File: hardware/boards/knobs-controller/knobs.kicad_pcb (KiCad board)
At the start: 2 copper layers, 110.5 x 54.3 mm, 70 parts, among them J1 ZX62-AB-5PA(31), J4 JST---S4B-PH-SM4-TB(LF)(SN)_J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, J8 2X3_SMD_MALE, SW1 Rotary Encoder, SW2 Rotary Encoder, SW3 Rotary Encoder, U2 AP7215-33YG-13, U3 ATSAMD21G18A-48, Y1 32.768KHz

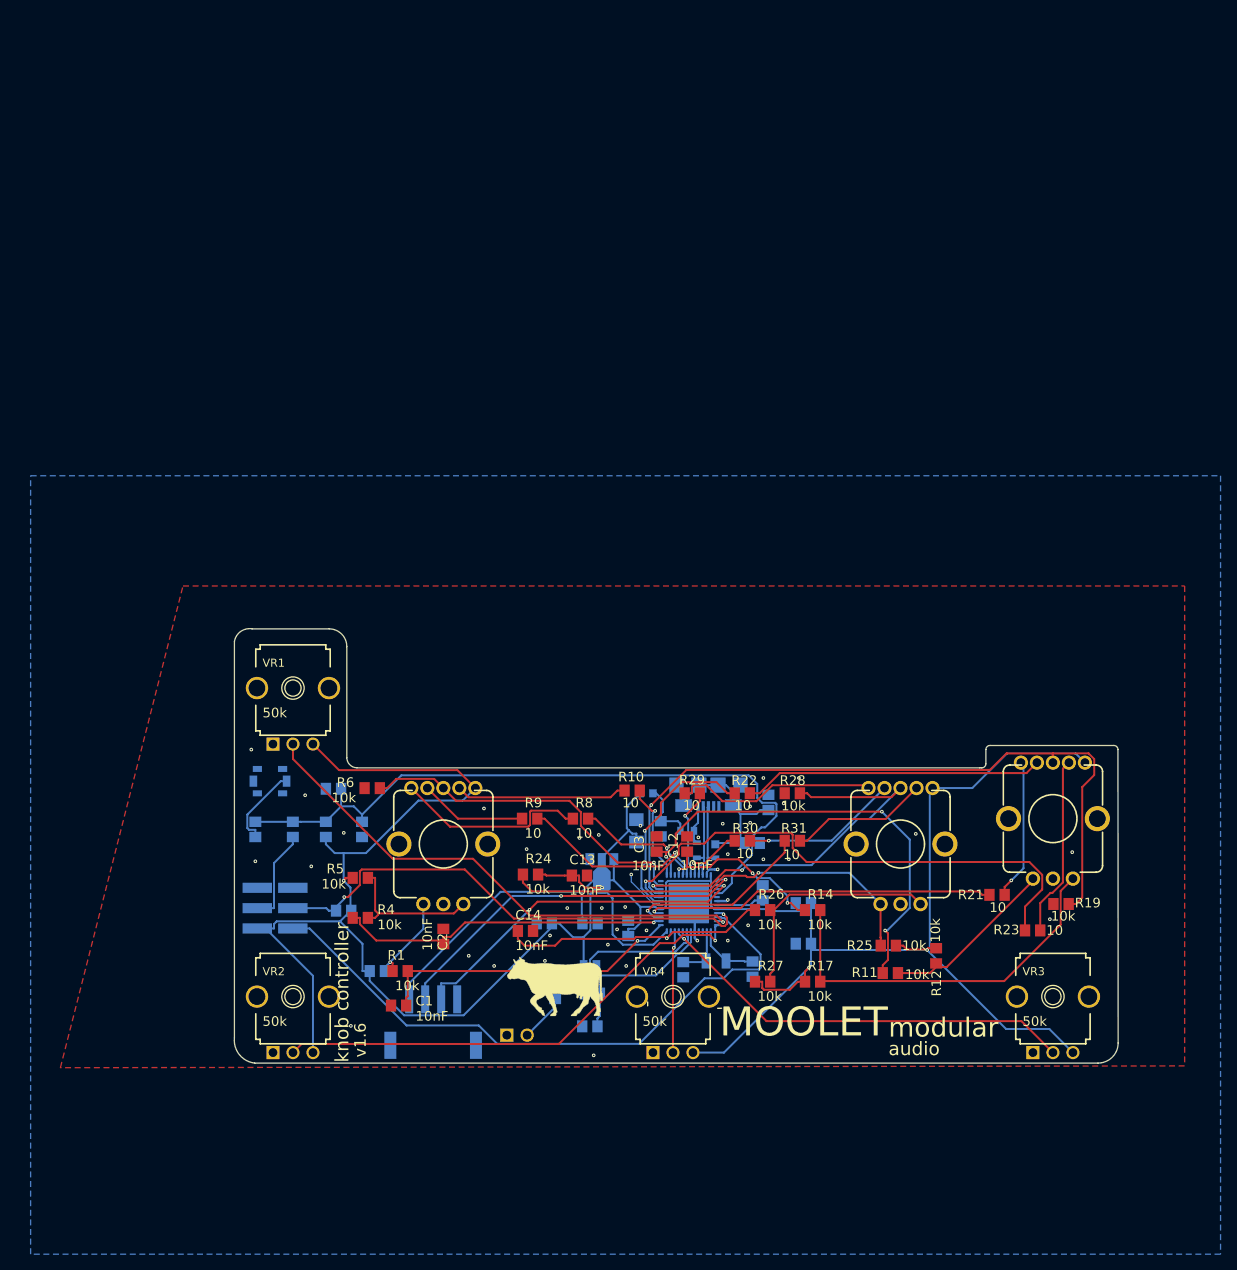
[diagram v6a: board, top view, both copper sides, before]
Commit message: v1.7: merge knobs and top breakout in to single board, remove fpc connector, replace with standard 0.1' pin header
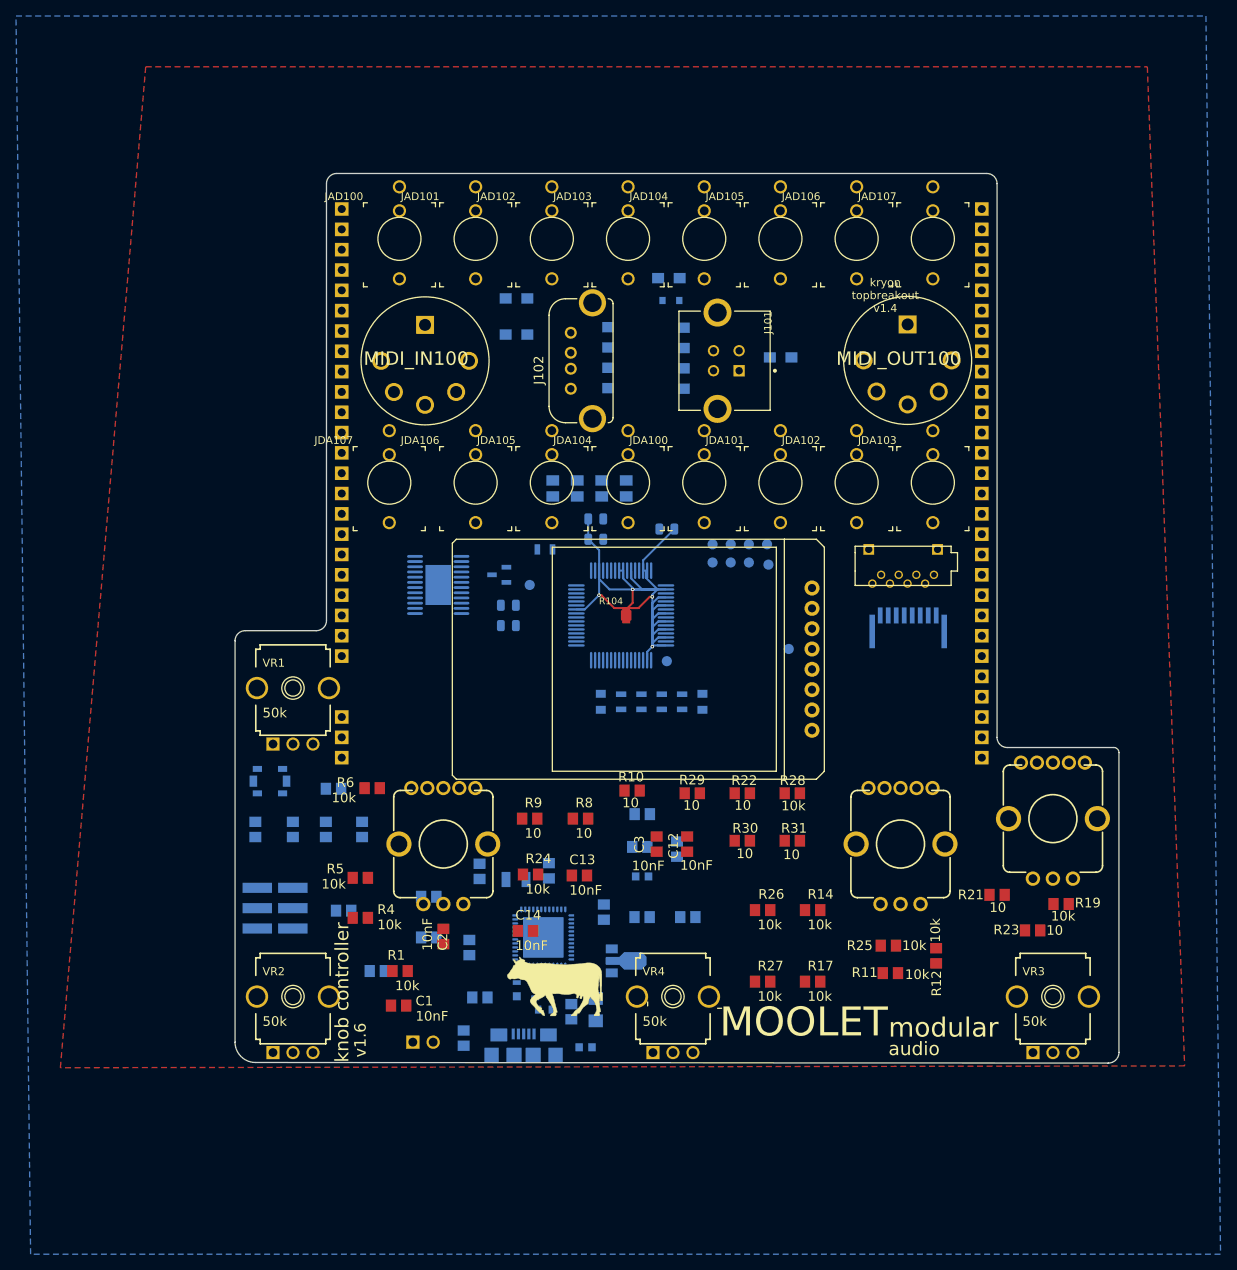
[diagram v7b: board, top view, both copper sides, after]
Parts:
- added C100: 0.1u, topbreakout:C0805K, B.Cu at (139.2, 60.3)
- added C101: 0.1u, topbreakout:C0805K, B.Cu at (136.1, 60.3)
- added C102: 0.1u, topbreakout:C0805K, B.Cu at (142.2, 60.3)
- added C103: 0.1u, topbreakout:C0805K, B.Cu at (133.1, 60.3)
- added C104: 10uF, Capacitor_SMD:C_0805_2012Metric, B.Cu at (147.3, 65.4)
- added C105: 1.0uF, Capacitor_SMD:C_0805_2012Metric, B.Cu at (138.4, 66.7)
- added C106: 1.0uF, Capacitor_SMD:C_0805_2012Metric, B.Cu at (138.4, 64.1)
- added C107: 0.1uF, Capacitors_SMD:C_0805, B.Cu at (139.1, 87.0)
- added C108: 0.1uF, Capacitors_SMD:C_0805, B.Cu at (151.8, 87.0)
- added C109: 0.1uF, Capacitor_SMD:C_0805_2012Metric, B.Cu at (127.5, 77.5)
- added C110: 0.1uF, Capacitor_SMD:C_0805_2012Metric, B.Cu at (127.5, 74.9)
- added D100: D, Diodes_SMD:D_0805, B.Cu at (147.8, 36.8)
- added J10: Conn_01x01_Female, Connector_PinSocket_2.54mm:PinSocket_1x01_P2.54mm_Vertical, B.Cu at (106.7, 48.3)
- added J101: WURTH_ELECTRONICS_61400413321WURTH_ELECTRONICS_61400413321_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, topbreakout:WURTH_ELECTRONICS_61400413321_0, F.Cu at (154.5, 44.4)
- added J102: USB-A-S-X-X-VT, topbreakout:USB-A-S-X-X-VT, F.Cu at (138.0, 44.4)
- added J103: ST7735_1.4, topbreakout:ST7735, F.Cu at (167.0, 66.7)
- added J11: Conn_01x01_Female, Connector_PinSocket_2.54mm:PinSocket_1x01_P2.54mm_Vertical, B.Cu at (186.7, 61.0)
- added J12: Conn_01x01_Female, Connector_PinSocket_2.54mm:PinSocket_1x01_P2.54mm_Vertical, B.Cu at (106.7, 63.5)
- added J13: Conn_01x01_Female, Connector_PinSocket_2.54mm:PinSocket_1x01_P2.54mm_Vertical, B.Cu at (106.7, 58.4)
- added J14: Conn_01x01_Female, Connector_PinSocket_2.54mm:PinSocket_1x01_P2.54mm_Vertical, B.Cu at (106.7, 81.3)
- added J15: Conn_01x01_Female, Connector_PinSocket_2.54mm:PinSocket_1x01_P2.54mm_Vertical, B.Cu at (106.7, 53.3)
- added J16: Conn_01x01_Female, Connector_PinSocket_2.54mm:PinSocket_1x01_P2.54mm_Vertical, B.Cu at (186.7, 76.2)
- added J17: Conn_01x01_Female, Connector_PinSocket_2.54mm:PinSocket_1x01_P2.54mm_Vertical, B.Cu at (186.7, 81.3)
- added J18: Conn_01x01_Female, Connector_PinSocket_2.54mm:PinSocket_1x01_P2.54mm_Vertical, B.Cu at (106.7, 66.0)
- added J19: Conn_01x01_Female, Connector_PinSocket_2.54mm:PinSocket_1x01_P2.54mm_Vertical, B.Cu at (186.7, 63.5)
- added J2: Conn_01x01_Female, Connector_PinSocket_2.54mm:PinSocket_1x01_P2.54mm_Vertical, B.Cu at (186.7, 50.8)
- added J20: Conn_01x01_Female, Connector_PinSocket_2.54mm:PinSocket_1x01_P2.54mm_Vertical, B.Cu at (186.7, 71.1)
- added J21: Conn_01x01_Female, Connector_PinSocket_2.54mm:PinSocket_1x01_P2.54mm_Vertical, B.Cu at (186.7, 68.6)
- added J22: Conn_01x01_Female, Connector_PinSocket_2.54mm:PinSocket_1x01_P2.54mm_Vertical, B.Cu at (186.7, 66.0)
- added J23: Conn_01x01_Female, Connector_PinSocket_2.54mm:PinSocket_1x01_P2.54mm_Vertical, B.Cu at (186.7, 73.7)
- added J24: Conn_01x01_Female, Connector_PinSocket_2.54mm:PinSocket_1x01_P2.54mm_Vertical, B.Cu at (106.7, 55.9)
- added J25: Conn_01x01_Female, Connector_PinSocket_2.54mm:PinSocket_1x01_P2.54mm_Vertical, B.Cu at (186.7, 83.8)
- added J26: Conn_01x01_Female, Connector_PinSocket_2.54mm:PinSocket_1x01_P2.54mm_Vertical, B.Cu at (186.7, 78.7)
- added J27: Conn_01x01_Female, Connector_PinSocket_2.54mm:PinSocket_1x01_P2.54mm_Vertical, B.Cu at (106.7, 61.0)
- added J28: Conn_01x01_Female, Connector_PinSocket_2.54mm:PinSocket_1x01_P2.54mm_Vertical, B.Cu at (106.7, 71.1)
- added J29: Conn_01x01_Female, Connector_PinSocket_2.54mm:PinSocket_1x01_P2.54mm_Vertical, B.Cu at (106.7, 73.7)
- added J3: Conn_01x01_Female, Connector_PinSocket_2.54mm:PinSocket_1x01_P2.54mm_Vertical, B.Cu at (186.7, 53.3)
- added J30: Conn_01x01_Female, Connector_PinSocket_2.54mm:PinSocket_1x01_P2.54mm_Vertical, B.Cu at (106.7, 68.6)
- added J31: Conn_01x01_Female, Connector_PinSocket_2.54mm:PinSocket_1x01_P2.54mm_Vertical, B.Cu at (106.7, 78.7)
- added J32: Conn_01x01_Female, Connector_PinSocket_2.54mm:PinSocket_1x01_P2.54mm_Vertical, B.Cu at (106.7, 76.2)
- added J33: Conn_01x01_Female, Connector_PinSocket_2.54mm:PinSocket_1x01_P2.54mm_Vertical, B.Cu at (186.7, 58.4)
- added J34: Conn_01x01_Female, Connector_PinSocket_2.54mm:PinSocket_1x01_P2.54mm_Vertical, B.Cu at (186.7, 94.0)
- added J35: Conn_01x01_Female, Connector_PinSocket_2.54mm:PinSocket_1x01_P2.54mm_Vertical, B.Cu at (186.7, 91.4)
- added J36: Conn_01x01_Female, Connector_PinSocket_2.54mm:PinSocket_1x01_P2.54mm_Vertical, B.Cu at (186.7, 88.9)
- added J37: Conn_01x01_Female, Connector_PinSocket_2.54mm:PinSocket_1x01_P2.54mm_Vertical, B.Cu at (186.7, 38.1)
- added J38: Conn_01x01_Female, Connector_PinSocket_2.54mm:PinSocket_1x01_P2.54mm_Vertical, B.Cu at (186.7, 40.6)
- added J39: Conn_01x01_Female, Connector_PinSocket_2.54mm:PinSocket_1x01_P2.54mm_Vertical, B.Cu at (186.7, 35.6)
- added J40: Conn_01x01_Female, Connector_PinSocket_2.54mm:PinSocket_1x01_P2.54mm_Vertical, B.Cu at (186.7, 43.2)
- added J41: Conn_01x01_Female, Connector_PinSocket_2.54mm:PinSocket_1x01_P2.54mm_Vertical, B.Cu at (186.7, 30.5)
- added J42: Conn_01x01_Female, Connector_PinSocket_2.54mm:PinSocket_1x01_P2.54mm_Vertical, B.Cu at (106.7, 88.9)
- added J43: Conn_01x01_Female, Connector_PinSocket_2.54mm:PinSocket_1x01_P2.54mm_Vertical, B.Cu at (186.7, 45.7)
- added J44: Conn_01x01_Female, Connector_PinSocket_2.54mm:PinSocket_1x01_P2.54mm_Vertical, B.Cu at (186.7, 33.0)
- added J45: Conn_01x01_Female, Connector_PinSocket_2.54mm:PinSocket_1x01_P2.54mm_Vertical, B.Cu at (106.7, 91.4)
- added J46: Conn_01x01_Female, Connector_PinSocket_2.54mm:PinSocket_1x01_P2.54mm_Vertical, B.Cu at (106.7, 27.9)
- added J47: Conn_01x01_Female, Connector_PinSocket_2.54mm:PinSocket_1x01_P2.54mm_Vertical, B.Cu at (186.7, 48.3)
- added J48: Conn_01x01_Female, Connector_PinSocket_2.54mm:PinSocket_1x01_P2.54mm_Vertical, B.Cu at (106.7, 94.0)
- added J49: Conn_01x01_Female, Connector_PinSocket_2.54mm:PinSocket_1x01_P2.54mm_Vertical, B.Cu at (106.7, 35.1)
- added J5: Conn_01x01_Female, Connector_PinSocket_2.54mm:PinSocket_1x01_P2.54mm_Vertical, B.Cu at (186.7, 55.9)
- added J50: Conn_01x01_Female, Connector_PinSocket_2.54mm:PinSocket_1x01_P2.54mm_Vertical, B.Cu at (106.7, 25.4)
- added J51: Conn_01x01_Female, Connector_PinSocket_2.54mm:PinSocket_1x01_P2.54mm_Vertical, B.Cu at (186.7, 25.4)
- added J52: Conn_01x01_Female, Connector_PinSocket_2.54mm:PinSocket_1x01_P2.54mm_Vertical, B.Cu at (106.7, 40.6)
- added J53: Conn_01x01_Female, Connector_PinSocket_2.54mm:PinSocket_1x01_P2.54mm_Vertical, B.Cu at (106.7, 33.0)
- added J54: Conn_01x01_Female, Connector_PinSocket_2.54mm:PinSocket_1x01_P2.54mm_Vertical, B.Cu at (106.7, 30.5)
- added J55: Conn_01x01_Female, Connector_PinSocket_2.54mm:PinSocket_1x01_P2.54mm_Vertical, B.Cu at (186.7, 27.9)
- added J56: Conn_01x01_Female, Connector_PinSocket_2.54mm:PinSocket_1x01_P2.54mm_Vertical, B.Cu at (106.7, 38.1)
- added J6: Conn_01x01_Female, Connector_PinSocket_2.54mm:PinSocket_1x01_P2.54mm_Vertical, B.Cu at (106.7, 45.7)
- added J7: Conn_01x01_Female, Connector_PinSocket_2.54mm:PinSocket_1x01_P2.54mm_Vertical, B.Cu at (106.7, 43.2)
- added J9: Conn_01x01_Female, Connector_PinSocket_2.54mm:PinSocket_1x01_P2.54mm_Vertical, B.Cu at (106.7, 50.8)
- added JAD100: THONKICONNNEW, topbreakout:WQP-PJ301M-12_JACK, F.Cu at (113.9, 29.1)
- added JAD101: THONKICONNNEW, topbreakout:WQP-PJ301M-12_JACK, F.Cu at (123.4, 29.1)
- added JAD102: THONKICONNNEW, topbreakout:WQP-PJ301M-12_JACK, F.Cu at (132.9, 29.1)
- added JAD103: THONKICONNNEW, topbreakout:WQP-PJ301M-12_JACK, F.Cu at (142.5, 29.1)
- added JAD104: THONKICONNNEW, topbreakout:WQP-PJ301M-12_JACK, F.Cu at (152.0, 29.1)
- added JAD105: THONKICONNNEW, topbreakout:WQP-PJ301M-12_JACK, F.Cu at (161.5, 29.1)
- added JAD106: THONKICONNNEW, topbreakout:WQP-PJ301M-12_JACK, F.Cu at (171.0, 29.1)
- added JAD107: THONKICONNNEW, topbreakout:WQP-PJ301M-12_JACK, F.Cu at (180.6, 29.1)
- added JDA100: THONKICONNNEW, topbreakout:WQP-PJ301M-12_JACK, F.Cu at (152.0, 59.6)
- added JDA101: THONKICONNNEW, topbreakout:WQP-PJ301M-12_JACK, F.Cu at (161.5, 59.6)
- added JDA102: THONKICONNNEW, topbreakout:WQP-PJ301M-12_JACK, F.Cu at (171.0, 59.6)
- added JDA103: THONKICONNNEW, topbreakout:WQP-PJ301M-12_JACK, F.Cu at (180.6, 59.6)
- added JDA104: THONKICONNNEW, topbreakout:WQP-PJ301M-12_JACK, F.Cu at (142.5, 59.6)
- added JDA105: THONKICONNNEW, topbreakout:WQP-PJ301M-12_JACK, F.Cu at (132.9, 59.6)
- added JDA106: THONKICONNNEW, topbreakout:WQP-PJ301M-12_JACK, F.Cu at (123.4, 59.6)
- added JDA107: THONKICONNNEW, topbreakout:WQP-PJ301M-12_JACK, F.Cu at (112.6, 59.6)
- added MIDI_IN100: OG-MIDI_MAB5SHCUI-SD-50BV, topbreakout:OG-MIDI_SD-50BV, F.Cu at (117.1, 44.4)
- added MIDI_OUT100: OG-MIDI_MAB5SHCUI-SD-50BV, topbreakout:OG-MIDI_SD-50BV, F.Cu at (177.4, 44.3)
- added R100: 4.7k, Resistors_SMD:R_0805, B.Cu at (141.6, 87.0)
- added R101: 4.7k, Resistors_SMD:R_0805, B.Cu at (149.2, 87.0)
- added R102: 4.7k, Resistors_SMD:R_0805, B.Cu at (144.1, 87.0)
- added R103: 4.7k, Resistors_SMD:R_0805, B.Cu at (146.7, 87.0)
- added R104: 0, Mainboard:NetTie-I_Connected_SMD_small, F.Cu at (142.2, 74.9)
- added R105: 4.7k, Resistors_SMD:R_0805, B.Cu at (132.1, 67.9)
- added R106: 220, Resistors_SMD:R_0805_HandSoldering, B.Cu at (128.5, 36.6)
- added R107: 220, Resistors_SMD:R_0805_HandSoldering, B.Cu at (147.6, 34.0)
- added R108: 220, Resistors_SMD:R_0805_HandSoldering, B.Cu at (161.5, 43.9)
- added R109: 220, Resistors_SMD:R_0805_HandSoldering, B.Cu at (128.5, 41.1)
- added TP100: TEST-POINT3X5, topbreakout:PAD.03X.05, B.Cu at (147.3, 81.9)
- added TP101: TEST-POINT3X5, topbreakout:PAD.03X.05, B.Cu at (153.0, 67.3)
- added TP102: TEST-POINT3X5, topbreakout:PAD.03X.05, B.Cu at (153.0, 69.6)
- added TP103: TEST-POINT3X5, topbreakout:PAD.03X.05, B.Cu at (155.3, 67.3)
- added TP104: TEST-POINT3X5, topbreakout:PAD.03X.05, B.Cu at (155.3, 69.6)
- added TP105: TEST-POINT3X5, topbreakout:PAD.03X.05, B.Cu at (157.6, 67.3)
- added TP106: TEST-POINT3X5, topbreakout:PAD.03X.05, B.Cu at (157.6, 69.6)
- added TP107: TEST-POINT3X5, topbreakout:PAD.03X.05, B.Cu at (159.8, 67.3)
- added TP108: TEST-POINT3X5, topbreakout:PAD.03X.05, B.Cu at (162.6, 80.4)
- added TP109: TEST-POINT3X5, topbreakout:PAD.03X.05, B.Cu at (160.0, 69.8)
- added TP110: TEST-POINT3X5, topbreakout:PAD.03X.05, B.Cu at (130.2, 72.4)
- added U$100: YAMAICHI_SD_CARD, topbreakout:YAMAICHI_MICROSD_VERTICAL, F.Cu at (176.9, 71.1)
- added U$101: 1734592-8, common:HFW8R-1STE1LF, B.Cu at (174.0, 76.2)
- added U$102: OPTO_DARL_6N138S, Mainboard:8-SMD, B.Cu at (144.5, 44.2)
- added U100: ANALOG_DEVICES_AD7606BSTZANALOG_DEVICES_AD7606BSTZ_0_2, topbreakout:ANALOG_DEVICES_AD7606BSTZ_2, B.Cu at (141.6, 76.2)
- added U101: ANALOG_DEVICES_AD5754BREZANALOG_DEVICES_AD5754BREZ_0_2, topbreakout:ANALOG_DEVICES_AD5754BREZ_2, B.Cu at (118.7, 72.4)
- added U102: MICROCHIP_MCP1700T-2502E-TTMICROCHIP_MCP1700T-2502E-TT_0_0, topbreakout:MICROCHIP_MCP1700T-2502E-TT_0, B.Cu at (126.4, 71.1)
- J4: value JST---S4B-PH-SM4-TB(LF)(SN)_JST_S4B-PH-SM4-TB_LF_SNJST_S4B-PH-SM4-TB_LF_SN_0_0 -> Conn_01x01_Female; footprint knobs:JST---S4B-PH-SM4-TB(LF)(SN)_JST_S4B-PH-SM4-TB_LF_SN_0 -> Connector_PinSocket_2.54mm:PinSocket_1x01_P2.54mm_Vertical
- moved J4 80.0 mm to (186.7, 86.4)
- moved R2 48.2 mm to (121.9, 129.0), turned to 90 degrees
- moved C28 47.2 mm to (117.6, 111.4), turned to 0 degrees
- moved C10 47.0 mm to (117.6, 116.4), turned to 0 degrees
- moved J1 41.5 mm to (129.4, 131.5), turned to 180 degrees
- moved C6 39.1 mm to (124.0, 124.0)
- moved C32 37.3 mm to (122.6, 117.7), turned to 270 degrees
- moved C11 36.3 mm to (123.9, 108.2), turned to 270 degrees
- moved L2 32.7 mm to (137.2, 130.2), turned to 0 degrees
- moved F2 28.6 mm to (132.1, 125.5), turned to 180 degrees
- moved D1 28.5 mm to (129.7, 123.0), turned to 0 degrees
- moved C30 27.3 mm to (144.2, 101.0), turned to 0 degrees
- moved Y1 27.0 mm to (128.5, 109.2), turned to 180 degrees
- moved C4 25.4 mm to (135.4, 125.7), turned to 90 degrees
- moved R18 23.4 mm to (148.6, 105.4), turned to 90 degrees
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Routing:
- net +3V3: track 305.3 -> 0.00 mm, vias 3 -> 0
- net AD_AGND: track 0.00 -> 93.6 mm, vias 0 -> 4
- net /knobs_1/PA12_S2_MOSI: track 91.6 -> 0.00 mm, vias 1 -> 0
- net /knobs_1/RESETN: track 88.9 -> 0.00 mm
- net /knobs_1/PA31_SWDIO: track 77.5 -> 0.00 mm
- net /knobs_1/PB11_TCC0-W5: track 66.9 -> 0.00 mm, vias 1 -> 0
- net /knobs_1/PB02_AIN10: track 64.9 -> 0.00 mm, vias 1 -> 0
- net /knobs_1/PA30_SWCLK: track 63.4 -> 0.00 mm, vias 2 -> 0
- net /knobs_1/PB03_AIN11: track 61.2 -> 0.00 mm, vias 1 -> 0
- net /knobs_1/PA17_S1_SCK: track 57.6 -> 0.00 mm, vias 3 -> 0
- net Net-(R24-Pad1): track 54.1 -> 0.00 mm, vias 1 -> 0
- net /knobs_1/PA04_AIN4: track 53.2 -> 0.00 mm, vias 1 -> 0
- net /knobs_1/PA13_S2_SCK: track 50.3 -> 0.00 mm, vias 2 -> 0
- net VIN: track 50.0 -> 0.00 mm
- net Net-(R14-Pad2): track 48.3 -> 0.00 mm
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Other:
- board size 110.5 x 54.3 mm -> 110.5 x 111.2 mm
- board text added: "22/12/2019"
- board text added: "3V3"
- board text added: "A/D"
- board text added: "AD5754"
- board text added: "AD7606"
- board text added: "AD_CONVST"
- board text added: "AD_CS"
- board text added: "AD_RESET"
- board text added: "AD_VREF"
- board text added: "AVDD"
- board text added: "AVIN"
- board text added: "D/A"
- board text added: "DA"
- board text added: "DA_SYNC"
- board text added: "GATE_1"
- board text added: "GATE_2"
- board text added: "GATE_3"
- board text added: "GATE_4"
- board text added: "MIDI_RX"
- board text added: "MIDI_TX"
- board text added: "MISO"
- board text added: "MOOLET instruments"
- board text added: "MOSI"
- board text added: "SCK"
- board text added: "TFT_CS"
- board text added: "TFT_DC"
- board text added: "Top breakout board"
- board text added: "USB_B D+"
- board text added: "USB_B D-"
- board text added: "USB_B VCC"
- board text added: "VIN"
- board text added: "VREF"
- board text added: "https://github.com/newdigate/teensy-eurorack"
- board text added: "kryon topbreakout v1.4"

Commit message: revised order of pin headers to make routing easier
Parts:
- moved J24 17.8 mm to (106.7, 73.7)
- moved J18 10.2 mm to (106.7, 55.9)
- moved J13 10.2 mm to (106.7, 68.6)
- moved J30 10.2 mm to (106.7, 58.4)
- moved J28 7.62 mm to (106.7, 63.5)
- moved J27 5.08 mm to (106.7, 66.0)
- moved J12 2.54 mm to (106.7, 61.0)
- moved J29 2.54 mm to (106.7, 71.1)
